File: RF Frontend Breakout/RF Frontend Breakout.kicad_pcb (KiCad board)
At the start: 2 copper layers, 122.5 x 83 mm, 54 parts, among them IC1 QPC1022SR, IC2 GRF5504, IC3 LHA-13LN+, IC4 QPC1022SR, J3 Conn_Coaxial, J4 Conn_01x02, J5 Conn_01x02, J6 Conn_Coaxial

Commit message: test
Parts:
- moved J3 109.9 mm to (193.3, 112.1), turned to 180 degrees
- moved J6 109.6 mm to (82.0, 120.6), turned to 0 degrees
- moved TP6 1.27 mm to (129.5, 87.5)
- moved IC3 1.25 mm to (157.5, 88.0)
- moved TP2 1.12 mm to (109.0, 87.5)
- moved FL2 1.02 mm to (119.1, 87.5)
- moved C5 0.93 mm to (141.2, 87.5)
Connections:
- C20 pad 1: Net-(J6-Ext) -> Net-(J6-In)
- J6 pad 1: GND -> Net-(J6-In)
- J6 pad 2: Net-(J6-Ext) -> GND
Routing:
- net Net-(FL2-RF_IN): track 0.00 -> 16.7 mm
- net Net-(IC4-ANT): track 10.7 -> 2.31 mm
- net Net-(FL2-RF_OUT): track 42.9 -> 43.7 mm

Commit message: finished pcb
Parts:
- moved C20 85.7 mm to (88.3, 120.5), turned to 0 degrees
- moved J4 48.6 mm to (90.5, 93.5)
- moved J5 37.0 mm to (87.5, 142.0)
- moved R1 25.9 mm to (108.5, 128.8), turned to 90 degrees
- moved TP3 25.1 mm to (103.5, 125.5)
- moved R2 24.6 mm to (112.8, 128.0)
- moved C3 18.2 mm to (114.5, 111.7)
- moved C1 17.0 mm to (101.0, 110.8), turned to 90 degrees
- moved TP7 16.3 mm to (167.5, 95.5)
- moved C16 13.8 mm to (164.5, 94.7)
- moved C11 13.6 mm to (154.0, 90.5), turned to 180 degrees
- moved R7 13.6 mm to (149.5, 90.5)
- moved L2 13.0 mm to (143.0, 94.1), turned to -90 degrees
- moved L6 12.4 mm to (161.0, 95.5), turned to 180 degrees
- moved C13 12.1 mm to (156.5, 95.5), turned to 180 degrees
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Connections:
- J4 pad 1: Net-(J4-Pin_1) -> +5V
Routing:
- net +5V: track 0.00 -> 251.2 mm, vias 0 -> 2
- net Net-(IC1-CTRL): track 0.00 -> 102.6 mm
- net GND: track 1.00 -> 52.7 mm, vias 1 -> 882
- net Net-(IC4-RF2): track 0.00 -> 34.8 mm, vias 0 -> 2
- net Net-(IC1-EN): track 0.00 -> 27.8 mm
- net /FEA09: track 0.00 -> 26.9 mm, vias 0 -> 1
- net Net-(IC3-RF-OUT&DC-IN): track 0.00 -> 19.7 mm
- net Net-(IC2-BIAS): track 0.00 -> 19.2 mm
- net Net-(IC4-ANT): track 2.31 -> 21.5 mm
- net Net-(IC4-RF1): track 23.7 -> 40.3 mm, vias 0 -> 2
- net Net-(IC4-EN): track 0.00 -> 13.4 mm
- net Net-(FL1-RF_OUT): track 5.23 -> 13.7 mm
- net Net-(IC3-RF-IN): track 0.00 -> 8.19 mm
- net Net-(FL2-RF_OUT): track 43.7 -> 35.7 mm
- net Net-(J6-In): track 0.00 -> 7.27 mm
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- added copper zone on F.Cu, net GND
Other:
- board text added: "+5V"

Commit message: small changes after larry meeting will populate his changes later
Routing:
- net GND: track 52.7 -> 56.9 mm, vias 882 -> 894
- net Net-(FL2-RF_OUT): track 35.7 -> 37.9 mm

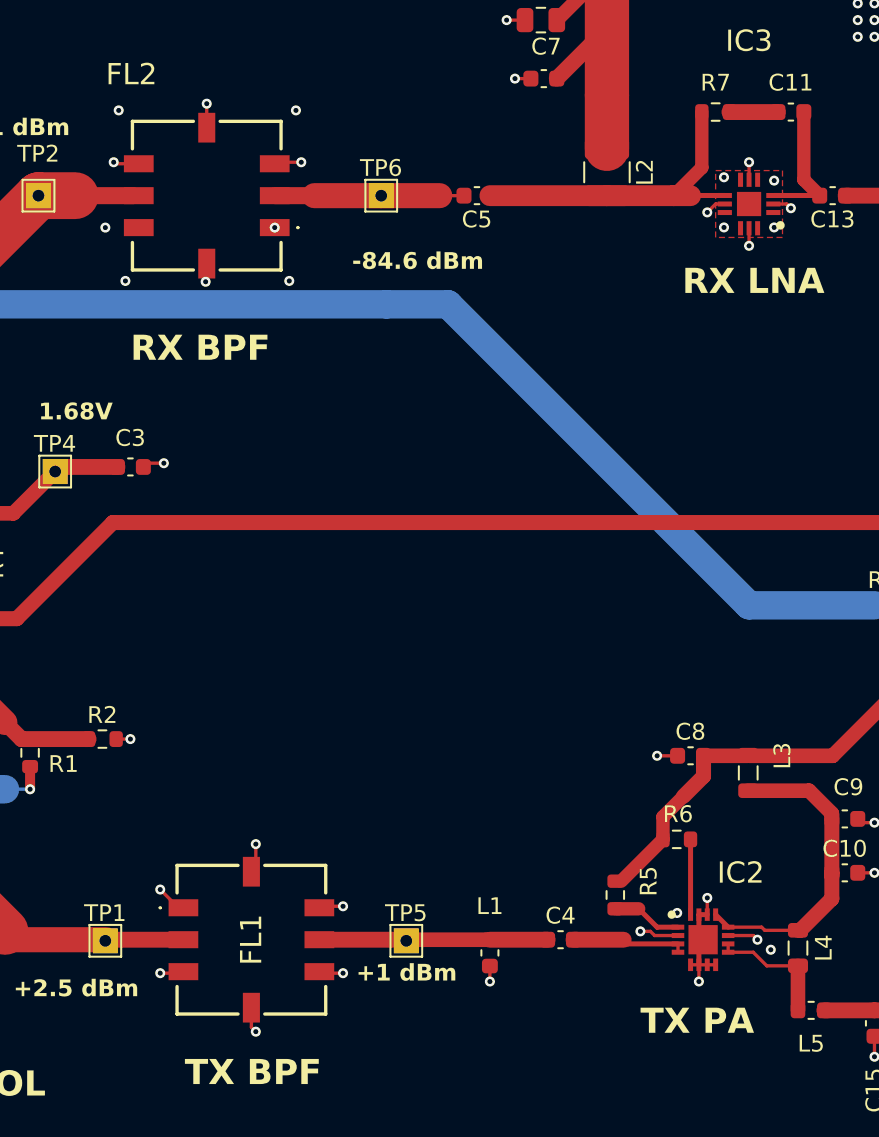
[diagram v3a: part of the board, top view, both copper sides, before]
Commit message: added groundplate to BPF and vias
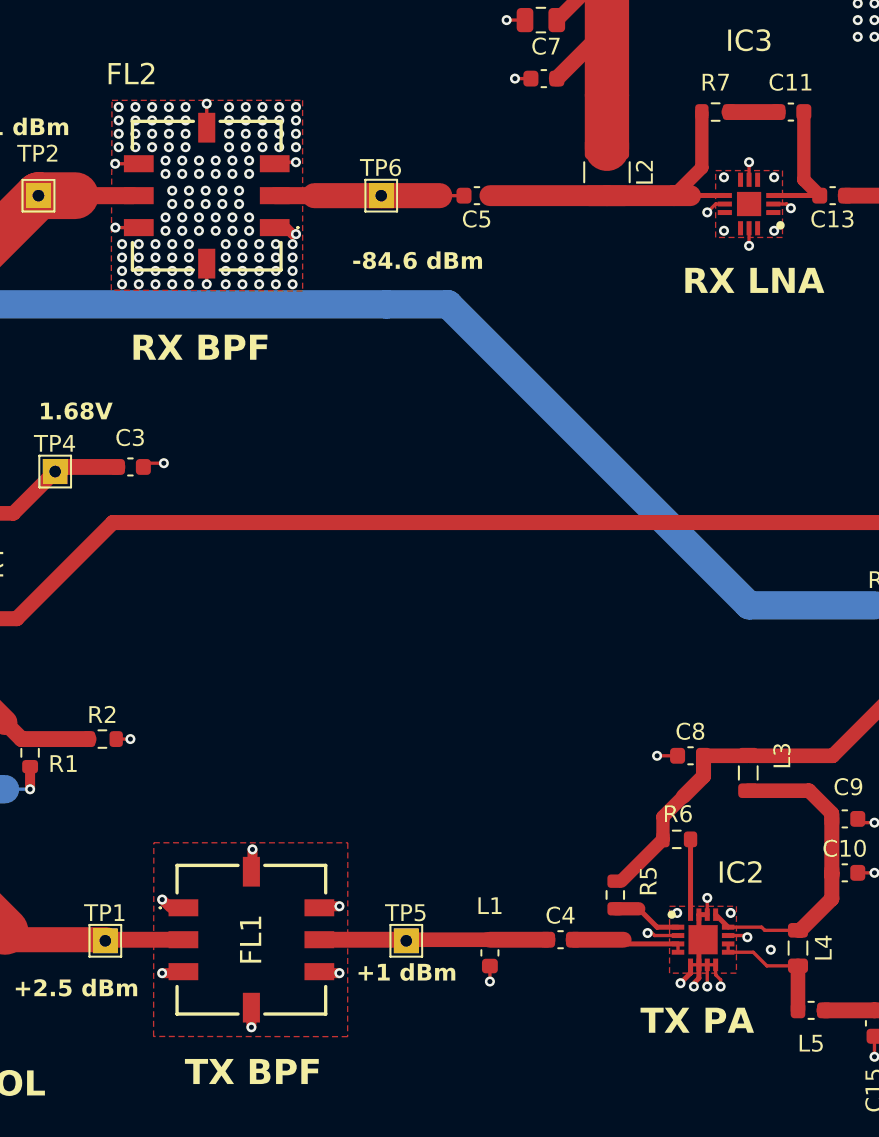
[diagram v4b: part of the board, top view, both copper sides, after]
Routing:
- net GND: track 56.9 -> 62.0 mm, vias 894 -> 1008

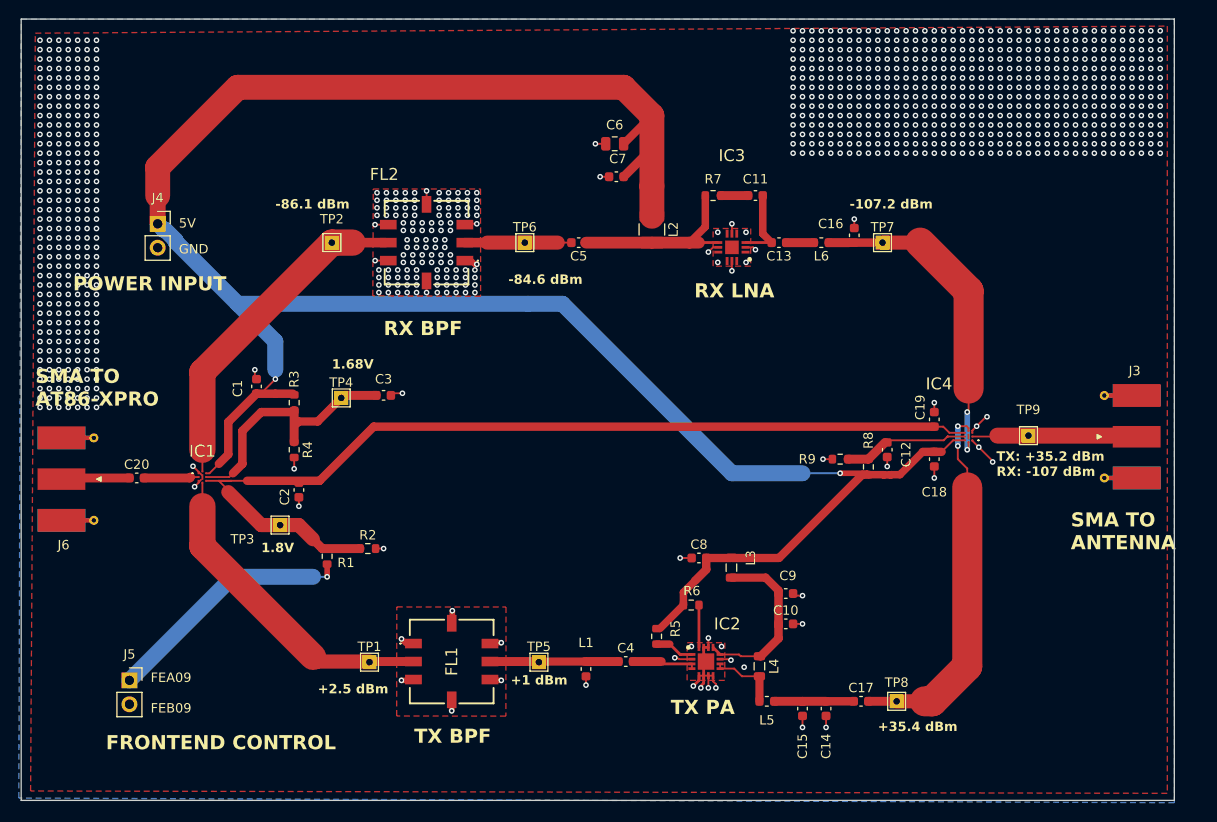
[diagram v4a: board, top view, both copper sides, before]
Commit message: brought power traces to front
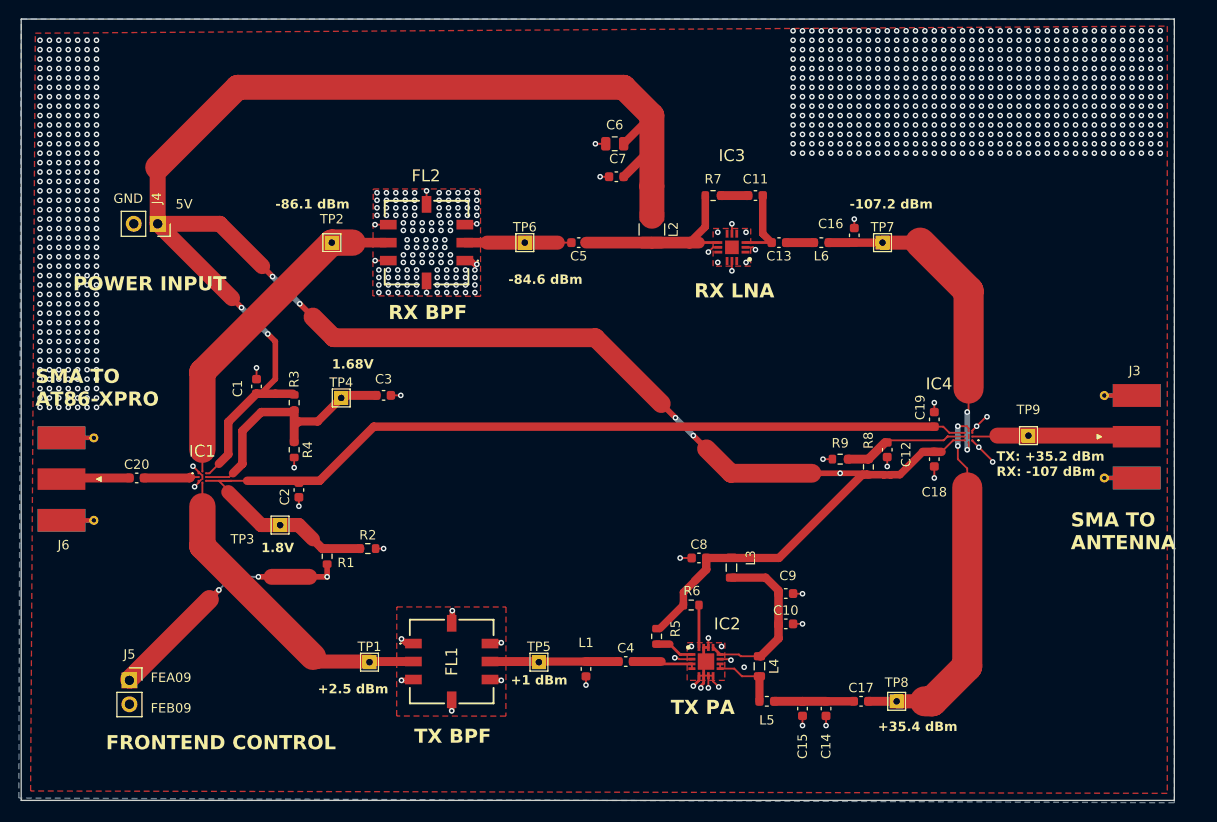
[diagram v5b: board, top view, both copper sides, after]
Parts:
- turned J4 to -90 degrees
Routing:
- net /FEA09: track 26.9 -> 27.0 mm, vias 1 -> 3
- net +5V: vias 2 -> 7
